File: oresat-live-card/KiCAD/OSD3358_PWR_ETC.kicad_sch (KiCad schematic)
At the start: 30 parts, among them Q1 MMBT2907, U10 TLVH431, U4 SN74LVC1G07DCK, U7 OSD3358-512M-BSM

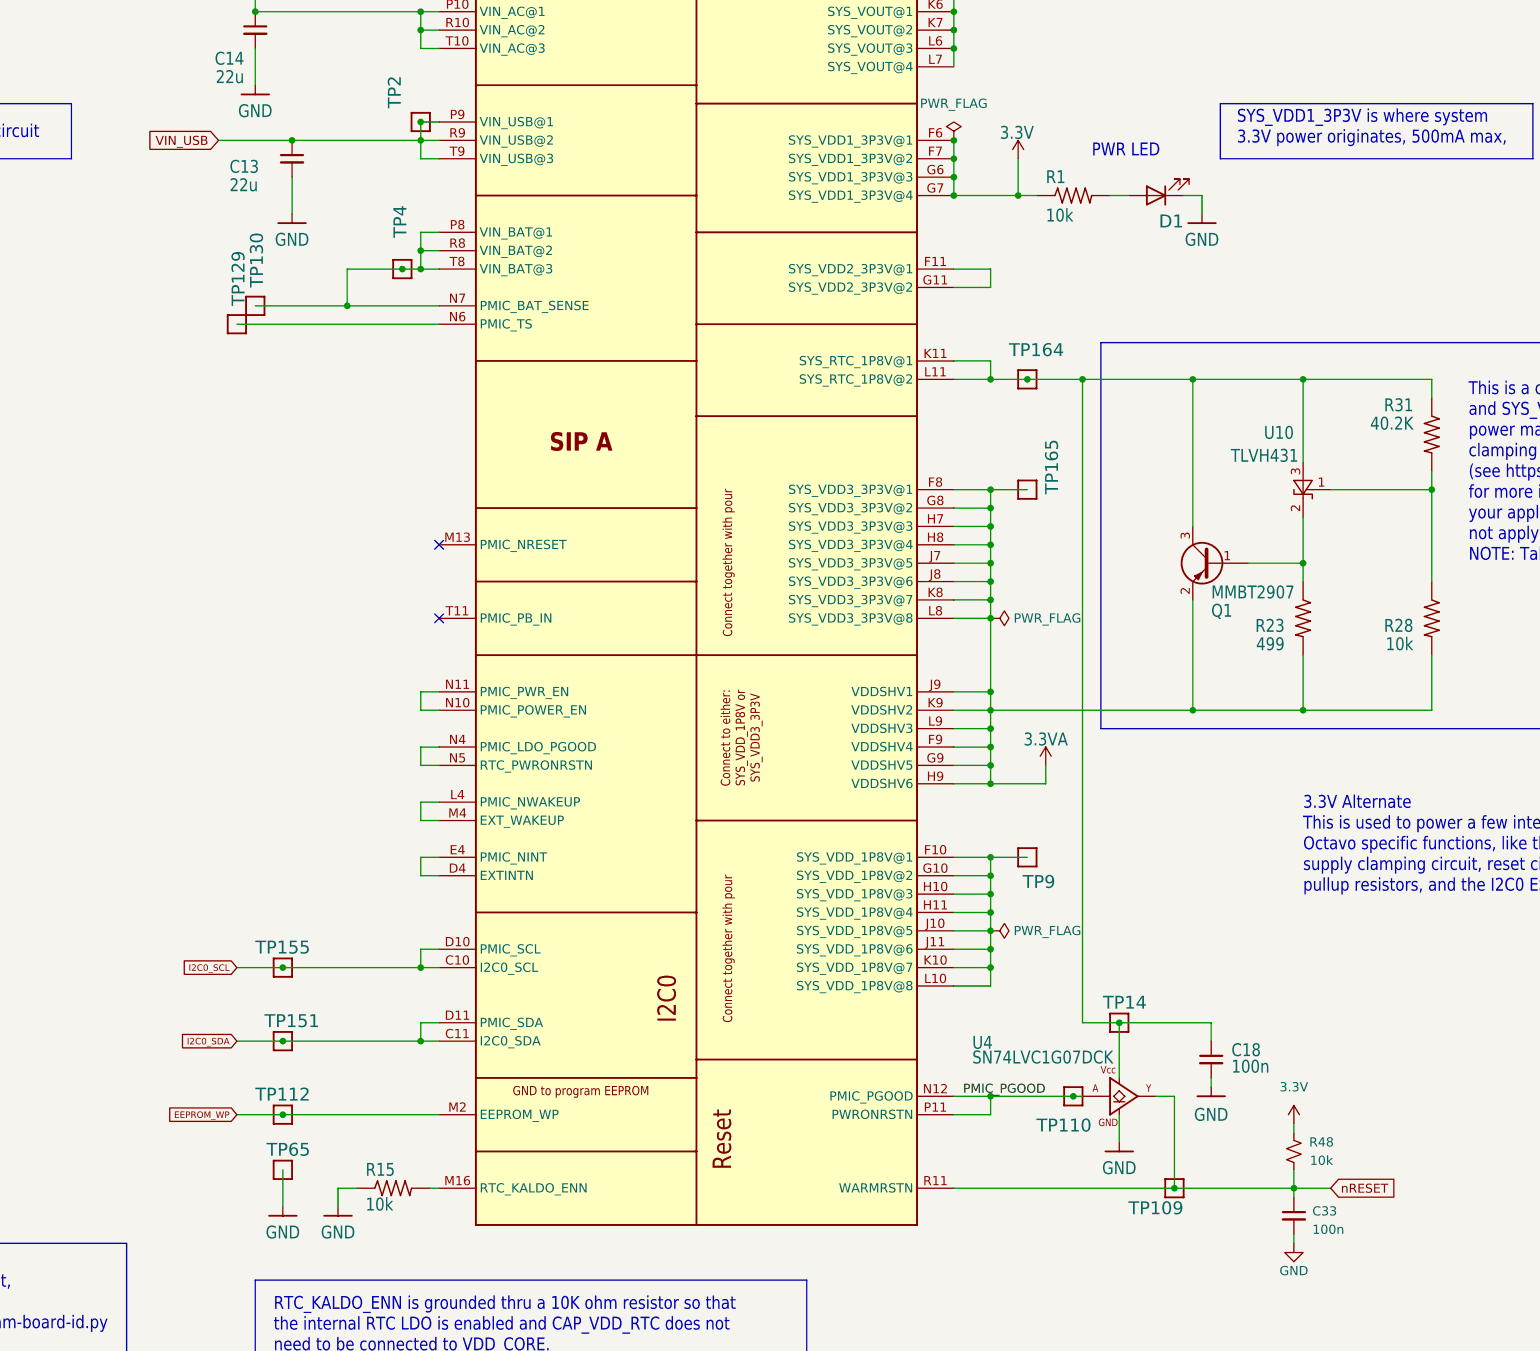
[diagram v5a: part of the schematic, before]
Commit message: added new sheets for LNA and switching
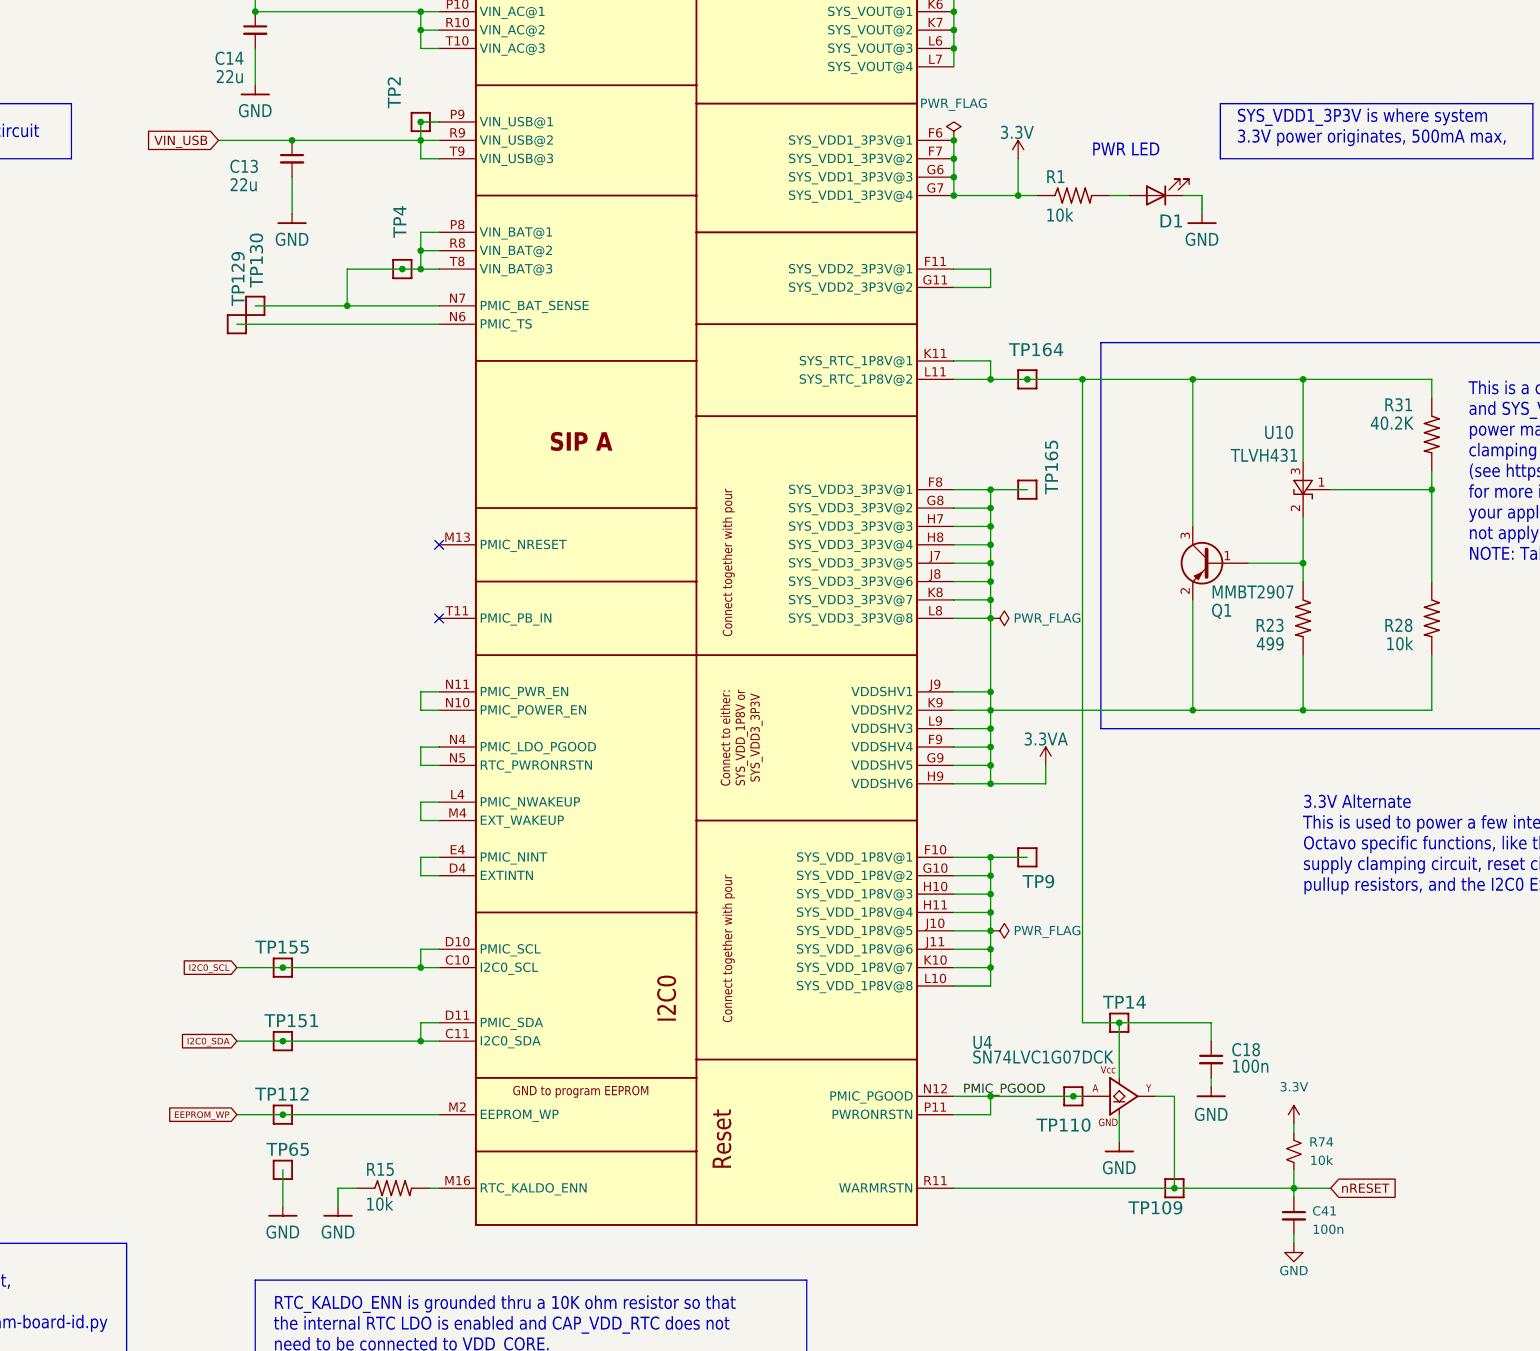
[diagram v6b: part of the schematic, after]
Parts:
- renumbered C33 to C41, R48 to R74
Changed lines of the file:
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@@
 (kicad_sch
-	(version 20231120)
+	(version 20250114)
 	(generator "eeschema")
-	(generator_version "8.0")
+	(generator_version "9.0")
 	(paper "B")
 	(title_block
@@
 		(rev "1.3")
 	)
+	(text "SYS_VOUT is the OR of \n5V from the bus and VIN_USB.\nImax = 500 mA"
+		(exclude_from_sim no)
+		(at 185.42 50.8 0)
+		(effects
+			(font
+				(size 1.27 1.27)
+			)
+			(justify left bottom)
+		)
+	)
+	(text "PWR LED"
+		(exclude_from_sim no)
+		(at 203.2 81.28 0)
+		(effects
+			(font
+				(size 1.778 1.5113)
+			)
+			(justify left bottom)
+		)
+	)
+	(text "RTC_KALDO_ENN is grounded thru a 10K ohm resistor so that\nthe internal RTC LDO is enabled and CAP_VDD_RTC does not\nneed to be connected to VDD_CORE."
+		(exclude_from_sim no)
+		(at 90.17 246.38 0)
+		(effects
+			(font
+				(size 1.778 1.5113)
+			)
+			(justify left bottom)
+		)
+	)
+	(text "SYS_VDD1_3P3V is where system\n3.3V power originates, 500mA max,"
+		(exclude_from_sim no)
+		(at 223.266 79.502 0)
+		(effects
+			(font
+				(size 1.778 1.5113)
+			)
+			(justify left bottom)
+		)
+	)
+	(text "PWR from USB client circuit"
+		(exclude_from_sim no)
+		(at 29.21 78.74 0)
+		(effects
+			(font
+				(size 1.778 1.5113)
+			)
+			(justify left bottom)
+		)
+	)
+	(text "This is a clamping circuit between the SYS_RTC_1P8V\nand SYS_VDD3_3P3V outputs of the TPS65217\npower management IC inside the OSD335x-SM.  The\nclamping circuit is related to power down issues\n(see https://octavosystems.com/osd335x/clamping/\nfor more information). This may not be needed in\nyour application if the power down conditions do\nnot apply to your application.\nNOTE: Taken verbatim from RED board"
+		(exclude_from_sim no)
+		(at 255.27 137.16 0)
+		(effects
+			(font
+				(size 1.778 1.5113)
+			)
+			(justify left bottom)
+		)
+	)
+	(text "3.3V Alternate\nThis is used to power a few internal and/or\nOctavo specific functions, like the power\nsupply clamping circuit, reset circuitry, I2C0\npullup resistors, and the I2C0 ESD protection"
+		(exclude_from_sim no)
+		(at 232.41 182.88 0)
+		(effects
+			(font
+				(size 1.778 1.5113)
+			)
+			(justify left bottom)
+		)
+	)
+	(text "Pull low to program EEPROM.\nProgram EEPROM with below script,\nusing another Pocketbeagle\noresat-star-tracker/utils/i2c-program-board-id.py"
+		(exclude_from_sim no)
+		(at 16.764 243.332 0)
+		(effects
+			(font
+				(size 1.778 1.5113)
+			)
+			(justify left bottom)
+		)
+	)
+	(text "Jumper to disconnect\noctavo from OPD power"
+		(exclude_from_sim no)
+		(at 54.61 43.18 0)
+		(effects
+			(font
+				(size 1.778 1.5113)
+			)
+			(justify left bottom)
+		)
+	)
 	(junction
 		(at 231.14 223.52)
@@
 		)
 	)
-	(text "SYS_VOUT is the OR of \n5V from the bus and VIN_USB.\nImax = 500 mA"
-		(exclude_from_sim no)
-		(at 185.42 50.8 0)
-		(effects
-			(font
-				(size 1.27 1.27)
-			)
-			(justify left bottom)
-		)
-	)
-	(text "PWR LED"
-		(exclude_from_sim no)
-		(at 203.2 81.28 0)
-		(effects
-			(font
-				(size 1.778 1.5113)
-			)
-			(justify left bottom)
-		)
-	)
-	(text "RTC_KALDO_ENN is grounded thru a 10K ohm resistor so that\nthe internal RTC LDO is enabled and CAP_VDD_RTC does not\nneed to be connected to VDD_CORE."
-		(exclude_from_sim no)
-		(at 90.17 246.38 0)
-		(effects
-			(font
-				(size 1.778 1.5113)
-			)
-			(justify left bottom)
-		)
-	)
-	(text "SYS_VDD1_3P3V is where system\n3.3V power originates, 500mA max,"
-		(exclude_from_sim no)
-		(at 223.266 79.502 0)
-		(effects
-			(font
-				(size 1.778 1.5113)
-			)
-			(justify left bottom)
-		)
-	)
-	(text "PWR from USB client circuit"
-		(exclude_from_sim no)
-		(at 29.21 78.74 0)
-		(effects
-			(font
-				(size 1.778 1.5113)
-			)
-			(justify left bottom)
-		)
-	)
-	(text "This is a clamping circuit between the SYS_RTC_1P8V\nand SYS_VDD3_3P3V outputs of the TPS65217\npower management IC inside the OSD335x-SM.  The\nclamping circuit is related to power down issues\n(see https://octavosystems.com/osd335x/clamping/\nfor more information). This may not be needed in\nyour application if the power down conditions do\nnot apply to your application.\nNOTE: Taken verbatim from RED board"
-		(exclude_from_sim no)
-		(at 255.27 137.16 0)
-		(effects
-			(font
-				(size 1.778 1.5113)
-			)
-			(justify left bottom)
-		)
-	)
-	(text "3.3V Alternate\nThis is used to power a few internal and/or\nOctavo specific functions, like the power\nsupply clamping circuit, reset circuitry, I2C0\npullup resistors, and the I2C0 ESD protection"
-		(exclude_from_sim no)
-		(at 232.41 182.88 0)
-		(effects
-			(font
-				(size 1.778 1.5113)
-			)
-			(justify left bottom)
-		)
-	)
-	(text "Pull low to program EEPROM.\nProgram EEPROM with below script,\nusing another Pocketbeagle\noresat-star-tracker/utils/i2c-program-board-id.py"
-		(exclude_from_sim no)
-		(at 16.764 243.332 0)
-		(effects
-			(font
-				(size 1.778 1.5113)
-			)
-			(justify left bottom)
-		)
-	)
-	(text "Jumper to disconnect\noctavo from OPD power"
-		(exclude_from_sim no)
-		(at 54.61 43.18 0)
-		(effects
-			(font
-				(size 1.778 1.5113)
-			)
-			(justify left bottom)
-		)
-	)
 	(label "PMIC_PGOOD"
 		(at 185.42 210.82 0)
-		(fields_autoplaced yes)
 		(effects
 			(font
@@
 		(effects
 			(font
-				(size 1.2446 1.2446)
+				(size 1.27 1.27)
 			)
 			(justify right)
 		)
 		(property "Intersheetrefs" "${INTERSHEET_REFS}"
-			(at 72.5398 78.6622 0)
+			(at 71.7633 78.74 0)
 			(effects
 				(font
@@
 		(effects
 			(font
-				(size 1.2446 1.2446)
+				(size 1.27 1.27)
 			)
 			(justify left)
 		)
 		(property "Intersheetrefs" "${INTERSHEET_REFS}"
-			(at 245.9017 223.52 0)
+			(at 246.0993 223.52 0)
 			(effects
 				(font
@@
 		(dnp no)
 		(fields_autoplaced yes)
-		(property "Reference" "#FLG02"
+		(property "Reference" "#FLG07"
 			(at 191.135 144.78 0)
 			(effects
@@
 		(dnp no)
 		(fields_autoplaced yes)
-		(property "Reference" "C33"
+		(property "Reference" "C41"
 			(at 233.68 226.7013 0)
 			(effects
@@
 		(dnp no)
 		(fields_autoplaced yes)
-		(property "Reference" "#FLG05"
+		(property "Reference" "#FLG09"
 			(at 184.15 76.835 0)
 			(effects
@@
 		(dnp no)
 		(fields_autoplaced yes)
-		(property "Reference" "#FLG02"
+		(property "Reference" "#FLG08"
 			(at 191.135 187.96 0)
 			(effects
@@
 		(on_board yes)
 		(dnp no)
-		(property "Reference" "R48"
+		(property "Reference" "R74"
 			(at 234.95 217.17 0)
 			(effects
